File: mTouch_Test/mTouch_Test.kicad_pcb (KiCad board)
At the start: 2 copper layers, 65.1 x 43.9 mm, 91 parts, among them J401 USB_B_Micro, J501 Prog, J601 Barrel_Jack_Switch, Q501 BSS214NW, Q601 Si2319CDS, U201 PIC18LF67K40-I_PT, U301 ISO7331C, U401 74LVC1G17, U402 FT234XD, U403 TPD3S014DBVR, U501 TL331, U502 74LVC1G86, U601 MCP1700-3302E

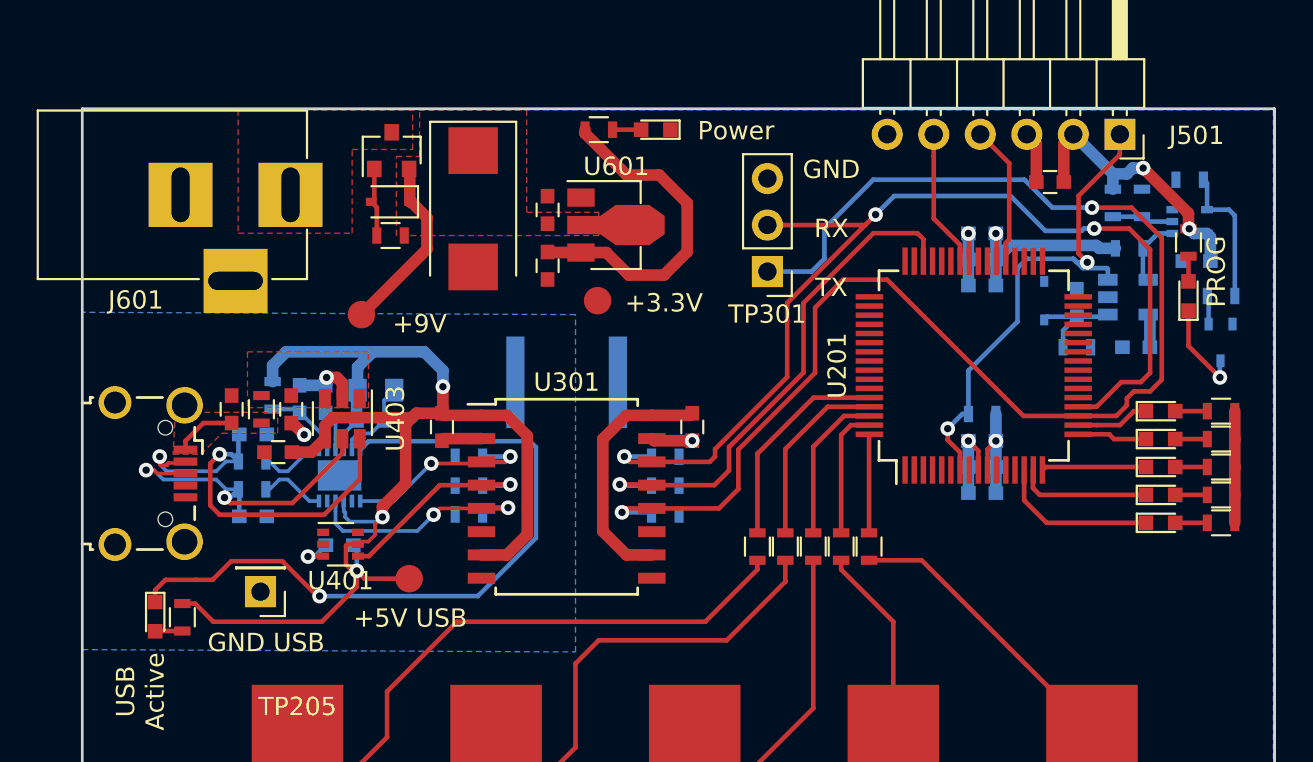
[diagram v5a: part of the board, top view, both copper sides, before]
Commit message: Finished Routing
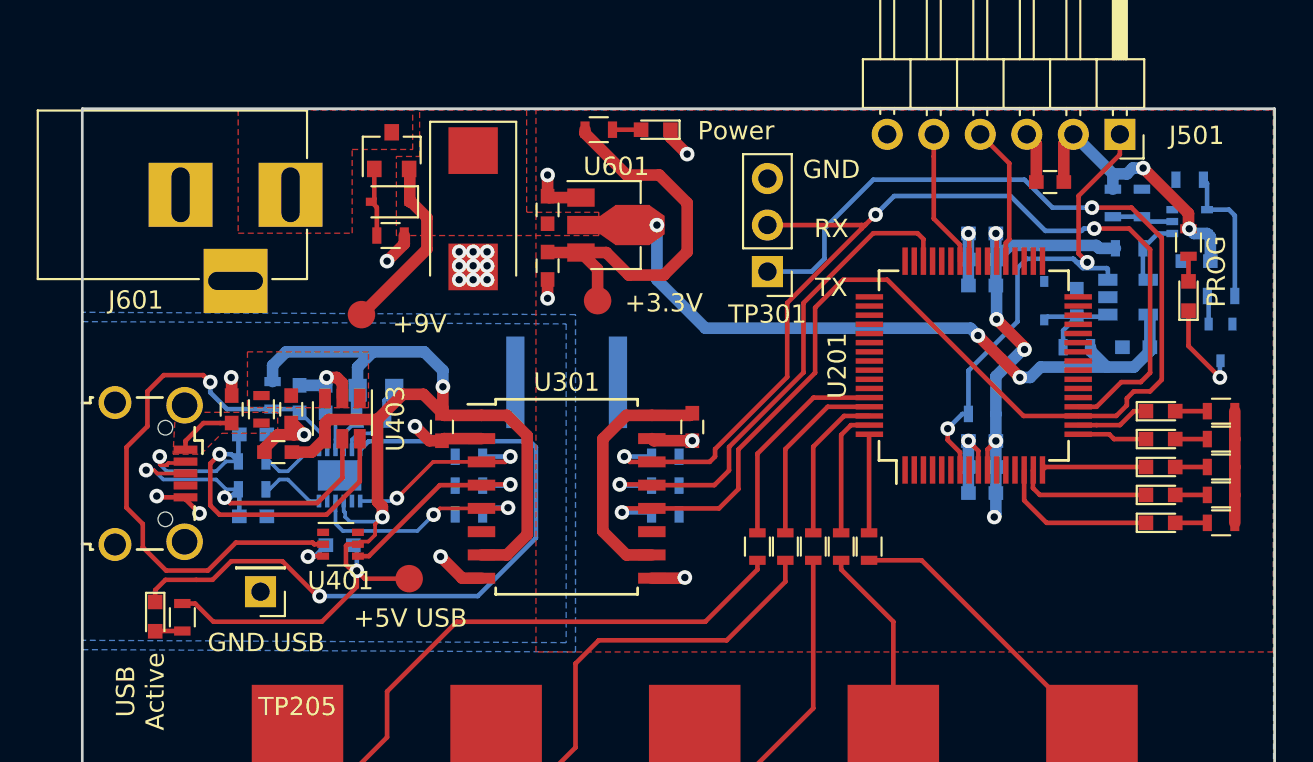
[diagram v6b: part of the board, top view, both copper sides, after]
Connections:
- J401 pad 6: Net-(J401-Pad6) -> (no net)
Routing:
- net +9V: track 17.1 -> 51.5 mm, vias 0 -> 3
- net Net-(C401-Pad1): track 4.23 -> 32.9 mm, vias 0 -> 1
- net +3V3: track 71.4 -> 84.1 mm, vias 4 -> 7
- net GND_USB: track 14.0 -> 25.0 mm, vias 3 -> 8
- net GND: track 14.1 -> 23.5 mm, vias 3 -> 17
- net /USB_UART_Converter/CONN_USB+: track 18.6 -> 19.4 mm
- added copper zone on F.Cu, net +3V3
- added copper zone on B.Cu, net GND_USB

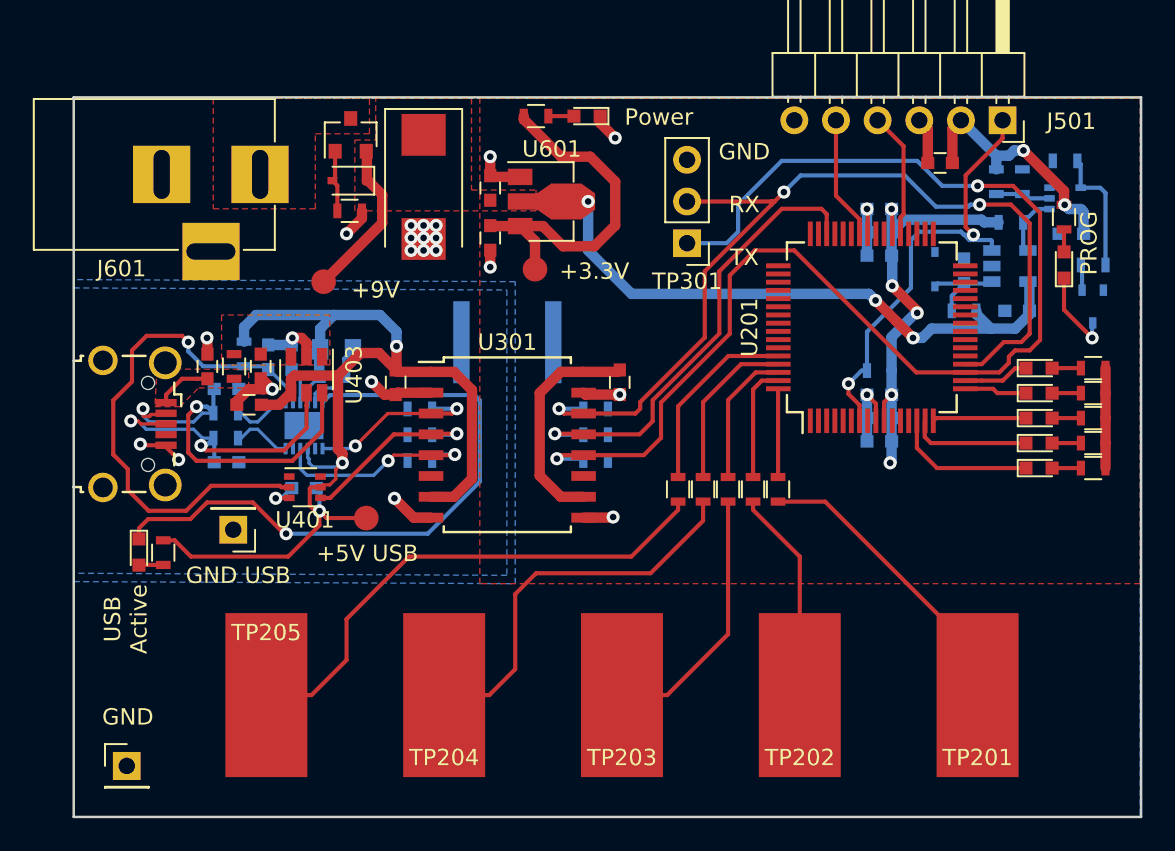
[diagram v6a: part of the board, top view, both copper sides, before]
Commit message: Changed +9V Net to +5V due to errors in LDO input voltage constraints
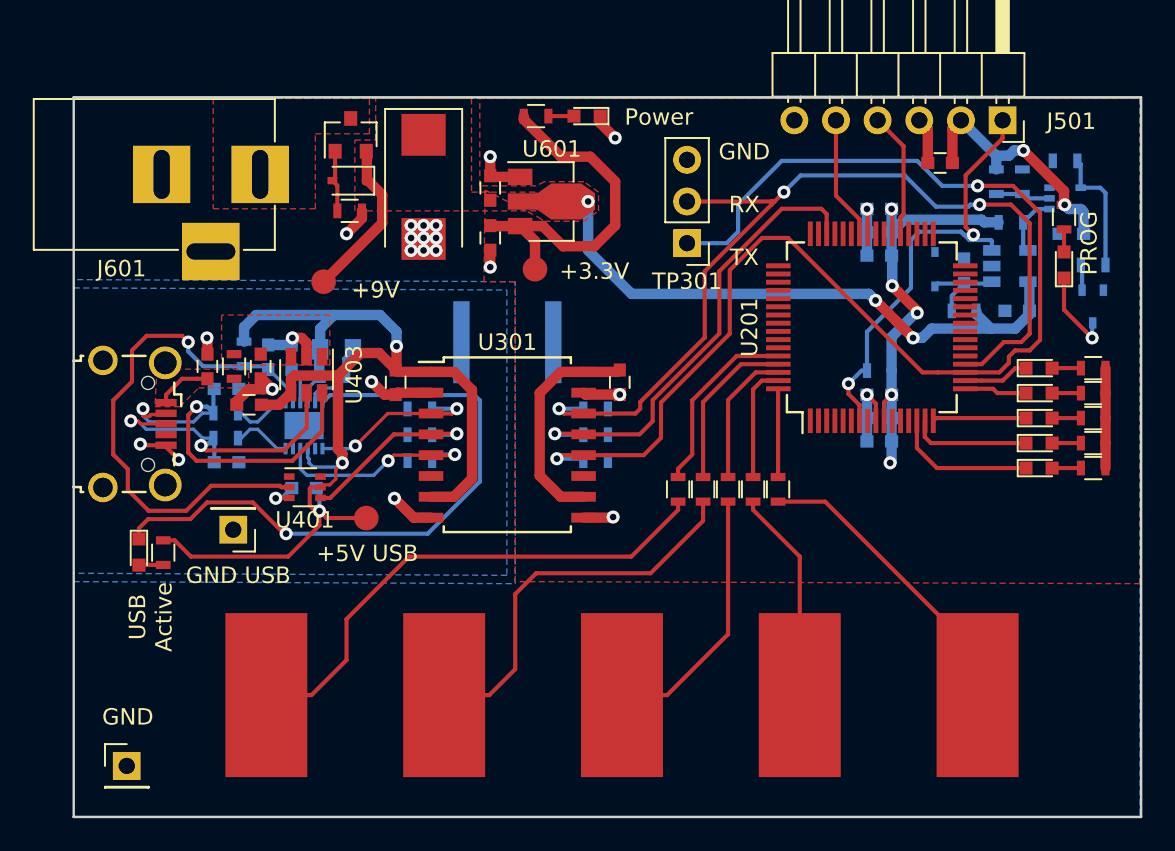
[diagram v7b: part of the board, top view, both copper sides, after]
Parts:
- turned TP205 to 180 degrees
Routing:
- net +9V: track 51.5 -> 56.7 mm
- net USB_UART_TX: track 77.5 -> 78.3 mm
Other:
- net class Default: clearance 0.2 -> 0.1524
- net class Power: clearance 0.2032 -> 0.1524
- net class Signal: clearance 0.2032 -> 0.1524
- rule trace_clearance: 0.2 -> 0.1524
- rule trace_min: 0.2 -> 0.1524
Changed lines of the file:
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@@
     (thickness 1.6)
     (drawings 14)
-    (tracks 570)
+    (tracks 575)
     (zones 0)
     (modules 91)
@@
   (setup
     (last_trace_width 0.25)
-    (trace_clearance 0.2)
+    (trace_clearance 0.1524)
     (zone_clearance 0.254)
     (zone_45_only no)
-    (trace_min 0.2)
+    (trace_min 0.1524)
     (segment_width 0.2)
     (edge_width 0.15)
@@
   (net 105 "Net-(U402-Pad8)")
   (net_class Default "This is the default net class."
-    (clearance 0.2)
+    (clearance 0.1524)
     (trace_width 0.25)
     (via_dia 0.8)
@@
   )
   (net_class Power ""
-    (clearance 0.2032)
+    (clearance 0.1524)
     (trace_width 0.635)
     (via_dia 0.8)
@@
   )
   (net_class Signal ""
-    (clearance 0.2032)
+    (clearance 0.1524)
     (trace_width 0.254)
     (via_dia 0.8)
@@
     (tags "MesurementPoint Square SMDPad 5mmx10mm ")
     (attr smd)
-    (fp_text reference TP201 (at 0 -3.81 180) (layer F.SilkS)
+    (fp_text reference TP201 (at 0 -3.81 180) (layer F.SilkS) hide
       (effects (font (size 1 1) (thickness 0.15)))
     )
@@
     (tags "MesurementPoint Square SMDPad 5mmx10mm ")
     (attr smd)
-    (fp_text reference TP202 (at 0 -3.81 180) (layer F.SilkS)
+    (fp_text reference TP202 (at 0 -3.81 180) (layer F.SilkS) hide
       (effects (font (size 1 1) (thickness 0.15)))
     )
@@
     (tags "MesurementPoint Square SMDPad 5mmx10mm ")
     (attr smd)
-    (fp_text reference TP203 (at 0 -3.81 180) (layer F.SilkS)
+    (fp_text reference TP203 (at 0 -3.81 180) (layer F.SilkS) hide
       (effects (font (size 1 1) (thickness 0.15)))
     )
@@
     (tags "MesurementPoint Square SMDPad 5mmx10mm ")
     (attr smd)
-    (fp_text reference TP204 (at 0 -3.81 180) (layer F.SilkS)
+    (fp_text reference TP204 (at 0 -3.81 180) (layer F.SilkS) hide
       (effects (font (size 1 1) (thickness 0.15)))
     )
@@
   )
   (module Wire_Pads:SolderWirePad_single_SMD_5x10mm (layer F.Cu)
-    (at 78.5495 133.2865)
+    (at 78.5495 133.2865 180)
     (descr "Wire Pad, Square, SMD Pad,  5mm x 10mm,")
     (tags "MesurementPoint Square SMDPad 5mmx10mm ")
     (attr smd)
-    (fp_text reference TP205 (at 0 -3.81) (layer F.SilkS)
+    (fp_text reference TP205 (at 0 -3.81 180) (layer F.SilkS) hide
       (effects (font (size 1 1) (thickness 0.15)))
     )
-    (fp_text value TP (at 0 6.35) (layer F.Fab)
+    (fp_text value TP (at 0 6.35 180) (layer F.Fab)
       (effects (font (size 1 1) (thickness 0.15)))
     )
@@
     (fp_line (start 2.75 5.25) (end 2.75 -5.25) (layer F.CrtYd) (width 0.05))
     (fp_line (start 2.75 -5.25) (end -2.75 -5.25) (layer F.CrtYd) (width 0.05))
-    (pad 1 smd rect (at 0 0) (size 5 10) (layers F.Cu)
+    (pad 1 smd rect (at 0 0 180) (size 5 10) (layers F.Cu)
       (net 45 "Net-(R206-Pad2)"))
   )
@@
     (effects (font (size 1 1) (thickness 0.15)))
   )
-  (gr_text "USB\nActive" (at 69.977 128.651 90) (layer F.SilkS)
+  (gr_text "USB\nActive" (at 71.501 128.524 90) (layer F.SilkS)
     (effects (font (size 1 1) (thickness 0.15)))
   )
@@
     (effects (font (size 1 1) (thickness 0.15)))
   )
-  (via (at 87.376 104.648) (size 0.8) (drill 0.4) (layers F.Cu B.Cu) (net 2))
   (segment (start 116.6756 117.8179) (end 116.6756 116.3955) (width 0.635) (layer B.Cu) (net 1))
   (segment (start 116.6756 116.3955) (end 116.6756 114.9731) (width 0.635) (layer B.Cu) (net 1))
@@
   (segment (start 116.713 106.5269) (end 116.6756 106.4895) (width 0.635) (layer B.Cu) (net 1))
   (segment (start 116.713 108.331) (end 116.713 106.5269) (width 0.635) (layer B.Cu) (net 1))
+  (via (at 87.376 104.648) (size 0.8) (drill 0.4) (layers F.Cu B.Cu) (net 2))
   (segment (start 115.1756 117.8179) (end 115.1756 116.3955) (width 0.635) (layer B.Cu) (net 2))
   (segment (start 115.1756 116.3955) (end 115.1756 114.9731) (width 0.635) (layer B.Cu) (net 2))
@@
   (segment (start 117.983 111.506) (end 118.548685 111.506) (width 0.635) (layer B.Cu) (net 12))
   (segment (start 118.548685 111.506) (end 119.114685 110.94) (width 0.635) (layer B.Cu) (net 12))
+  (segment (start 94.1705 103.1875) (end 95.4278 103.1875) (width 0.635) (layer F.Cu) (net 12))
+  (segment (start 94.1705 103.1875) (end 98.171 103.1875) (width 0.635) (layer F.Cu) (net 12))
   (segment (start 126.4665 113.3475) (end 128.2185 113.3475) (width 0.254) (layer F.Cu) (net 13))
   (segment (start 122.1724 114.1083) (end 121.1684 114.1083) (width 0.254) (layer F.Cu) (net 14))
@@
   (segment (start 87.249 124.841) (end 100.8093 124.841) (width 0.254) (layer F.Cu) (net 45))
   (segment (start 83.439 128.651) (end 87.249 124.841) (width 0.254) (layer F.Cu) (net 45))
-  (segment (start 103.6574 119.9889) (end 103.6574 115.6716) (width 0.254) (layer F.Cu) (net 46))
-  (segment (start 106.7207 112.6083) (end 109.7684 112.6083) (width 0.254) (layer F.Cu) (net 46))
-  (segment (start 103.6574 115.6716) (end 106.7207 112.6083) (width 0.254) (layer F.Cu) (net 46))
+  (segment (start 107.2287 112.6083) (end 109.7684 112.6083) (width 0.254) (layer F.Cu) (net 46))
+  (segment (start 104.521 115.316) (end 107.2287 112.6083) (width 0.254) (layer F.Cu) (net 46))
+  (segment (start 104.521 118.6213) (end 104.521 115.316) (width 0.254) (layer F.Cu) (net 46))
+  (segment (start 103.6574 119.9889) (end 103.6574 119.4849) (width 0.254) (layer F.Cu) (net 46))
+  (segment (start 103.6574 119.4849) (end 104.521 118.6213) (width 0.254) (layer F.Cu) (net 46))
   (via (at 96.139 117.348) (size 0.8) (drill 0.4) (layers F.Cu B.Cu) (net 47))
   (segment (start 97.8782 117.4115) (end 96.2025 117.4115) (width 0.254) (layer B.Cu) (net 47))
@@
   (segment (start 125.095 112.268) (end 124.206 112.268) (width 0.254) (layer F.Cu) (net 48))
   (segment (start 124.206 112.268) (end 123.825 112.649) (width 0.254) (layer F.Cu) (net 48))
-  (segment (start 118.1803 113.6083) (end 121.1684 113.6083) (width 0.254) (layer F.Cu) (net 48))
-  (segment (start 110.744 106.172) (end 118.1803 113.6083) (width 0.254) (layer F.Cu) (net 48))
-  (segment (start 108.331 106.172) (end 110.744 106.172) (width 0.254) (layer F.Cu) (net 48))
-  (segment (start 101.5619 118.6561) (end 102.616 117.602) (width 0.254) (layer F.Cu) (net 48))
+  (segment (start 118.5613 113.6083) (end 119.507 113.6083) (width 0.254) (layer F.Cu) (net 48))
+  (segment (start 110.363 105.41) (end 118.5613 113.6083) (width 0.254) (layer F.Cu) (net 48))
+  (segment (start 108.77875 105.41) (end 110.363 105.41) (width 0.254) (layer F.Cu) (net 48))
+  (segment (start 119.507 113.6083) (end 121.1684 113.6083) (width 0.254) (layer F.Cu) (net 48))
   (segment (start 97.8934 118.6561) (end 101.5619 118.6561) (width 0.254) (layer F.Cu) (net 48))
+  (segment (start 106.807 107.38175) (end 108.77875 105.41) (width 0.254) (layer F.Cu) (net 48))
+  (segment (start 101.5619 118.6561) (end 102.616 117.602) (width 0.254) (layer F.Cu) (net 48))
   (segment (start 102.616 117.602) (end 102.616 115.443) (width 0.254) (layer F.Cu) (net 48))
+  (segment (start 106.807 111.252) (end 106.807 107.38175) (width 0.254) (layer F.Cu) (net 48))
   (segment (start 102.616 115.443) (end 106.807 111.252) (width 0.254) (layer F.Cu) (net 48))
-  (segment (start 106.807 111.252) (end 106.807 107.696) (width 0.254) (layer F.Cu) (net 48))
-  (segment (start 106.807 107.696) (end 108.331 106.172) (width 0.254) (layer F.Cu) (net 48))
   (via (at 96.393 115.824) (size 0.8) (drill 0.4) (layers F.Cu B.Cu) (net 49))
   (segment (start 97.8934 116.1161) (end 96.6851 116.1161) (width 0.254) (layer F.Cu) (net 49))
@@
     (polygon
       (pts
-        (xy 83.947 99.441) (xy 85.217 99.441) (xy 85.217 96.901) (xy 91.059 96.901) (xy 91.059 102.489)
-        (xy 94.996 102.489) (xy 94.996 103.759) (xy 83.947 103.759)
+        (xy 83.947 99.441) (xy 85.217 99.441) (xy 85.217 96.901) (xy 91.059 96.901) (xy 91.059 102.616)
+        (xy 94.996 102.616) (xy 94.996 103.759) (xy 83.947 103.759)
       )
     )
@@
     (polygon
       (pts
-        (xy 91.567 96.901) (xy 131.826 96.901) (xy 131.826 126.492) (xy 91.567 126.492)
+        (xy 98.806 103.759) (xy 98.806 102.616) (xy 97.917 101.981) (xy 95.504 101.981) (xy 94.996 102.235)
+        (xy 91.567 102.235) (xy 91.567 96.901) (xy 131.826 96.901) (xy 131.826 126.492) (xy 93.726 126.365)
+        (xy 93.726 108.077) (xy 91.821 108.077) (xy 91.884503 102.488639) (xy 95.123 104.14) (xy 95.504 104.394)
+        (xy 97.917 104.394)
       )
     )
